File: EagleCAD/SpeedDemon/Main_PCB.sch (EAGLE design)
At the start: 68 parts, among them Q1 DMC2700, U3 LM3676, U4 STM32F072-LQFP48, X1 32.768kHz

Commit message: Draft layout. Moved power reg circuit as far away from everything else as possible to minimize possible noise issues. Also poured polygons for power planes
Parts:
- removed C17: 100nF, rcl:C-US025-024X044
- removed SIGNAL_OP: (no value), wirepad:1,6/0,8
- removed U1A: (no value), US5881:US5881
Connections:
- removed net N$37: SIGNAL_OP.P, U1A.OP
- net GND: no longer C17.2, U1A.VSS
- net VBATT+_SW: no longer C17.1, U1A.VDD
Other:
- note removed: "*NOTE: No PCB for this portion of circuit! Use point-to-point wiring."
- note removed: "3-Conductor cable run"
- note removed: "Sensor module"
- note removed: "Use Mogami W2944 Balanced Console Cable or similar (tie gnd to cable shield)"
- note removed: "XLR-F Cable0 mount conn"
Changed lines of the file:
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@@
 <part name="R32" library="0805_generics" deviceset="R_0805" device="" value="10k"/>
 <part name="GND22" library="supply1" library_urn="urn:adsk.eagle:library:371" deviceset="GND" device=""/>
-<part name="GND23" library="supply1" library_urn="urn:adsk.eagle:library:371" deviceset="GND" device=""/>
-<part name="VBATT_SW3" library="Custom_Power_Inlets" deviceset="VBATT+_SW" device=""/>
-<part name="SIGNAL_OP" library="wirepad" library_urn="urn:adsk.eagle:library:412" deviceset="1,6/0,8" device="" package3d_urn="urn:adsk.eagle:package:30830/1"/>
-<part name="C17" library="rcl" library_urn="urn:adsk.eagle:library:334" deviceset="C-US" device="025-024X044" package3d_urn="urn:adsk.eagle:package:23630/1" value="100nF"/>
-<part name="U1A" library="US5881" deviceset="US5881" device=""/>
-<part name="FRAME2" library="frames" library_urn="urn:adsk.eagle:library:229" deviceset="A3L-LOC" device=""/>
 <part name="C6" library="LCRD_SMD_generics" deviceset="C_0805_NP" device="" value="22pF"/>
 <part name="C18" library="LCRD_SMD_generics" deviceset="C_0805_NP" device="" value="22pF"/>
@@
 </segment>
 </net>
-</nets>
-</sheet>
-<sheet>
-<plain>
-<wire x1="168.275" y1="246.38" x2="168.275" y2="195.58" width="0.1524" layer="97"/>
-<wire x1="168.275" y1="195.58" x2="192.405" y2="195.58" width="0.1524" layer="97"/>
-<wire x1="192.405" y1="195.58" x2="192.405" y2="246.38" width="0.1524" layer="97"/>
-<wire x1="192.405" y1="246.38" x2="168.275" y2="246.38" width="0.1524" layer="97"/>
-<wire x1="103.505" y1="237.49" x2="103.505" y2="203.2" width="0.1524" layer="97"/>
-<wire x1="103.505" y1="203.2" x2="136.525" y2="203.2" width="0.1524" layer="97"/>
-<wire x1="136.525" y1="203.2" x2="136.525" y2="237.49" width="0.1524" layer="97"/>
-<wire x1="136.525" y1="237.49" x2="122.555" y2="237.49" width="0.1524" layer="97"/>
-<text x="104.775" y="238.76" size="1.778" layer="97">Sensor module</text>
-<text x="169.545" y="247.65" size="1.778" layer="97">XLR-F
-Cable0 mount conn</text>
-<wire x1="122.555" y1="237.49" x2="103.505" y2="237.49" width="0.1524" layer="97"/>
-<wire x1="168.275" y1="246.38" x2="168.275" y2="252.73" width="0.1524" layer="97"/>
-<wire x1="168.275" y1="252.73" x2="192.405" y2="252.73" width="0.1524" layer="97"/>
-<wire x1="192.405" y1="252.73" x2="192.405" y2="246.38" width="0.1524" layer="97"/>
-<wire x1="103.505" y1="237.49" x2="103.505" y2="241.3" width="0.1524" layer="97"/>
-<wire x1="103.505" y1="241.3" x2="122.555" y2="241.3" width="0.1524" layer="97"/>
-<wire x1="122.555" y1="241.3" x2="122.555" y2="237.49" width="0.1524" layer="97"/>
-<wire x1="141.605" y1="227.33" x2="141.605" y2="214.63" width="0.1524" layer="97"/>
-<wire x1="141.605" y1="214.63" x2="163.195" y2="214.63" width="0.1524" layer="97"/>
-<wire x1="163.195" y1="214.63" x2="163.195" y2="227.33" width="0.1524" layer="97"/>
-<wire x1="163.195" y1="227.33" x2="156.845" y2="227.33" width="0.1524" layer="97"/>
-<text x="142.875" y="228.6" size="1.778" layer="97">3-Conductor
-cable run</text>
-<wire x1="156.845" y1="227.33" x2="141.605" y2="227.33" width="0.1524" layer="97"/>
-<wire x1="141.605" y1="227.33" x2="141.605" y2="234.95" width="0.1524" layer="97"/>
-<wire x1="141.605" y1="234.95" x2="156.845" y2="234.95" width="0.1524" layer="97"/>
-<wire x1="156.845" y1="234.95" x2="156.845" y2="227.33" width="0.1524" layer="97"/>
-<text x="142.24" y="209.55" size="1.016" layer="97">Use Mogami W2944
-Balanced Console Cable or similar
-(tie gnd to cable shield)</text>
-<text x="98.425" y="253.365" size="1.6764" layer="97">*NOTE: No PCB for this portion of circuit! Use point-to-point wiring.</text>
-</plain>
-<instances>
-<instance part="GND23" gate="1" x="187.325" y="203.2"/>
-<instance part="VBATT_SW3" gate="G$1" x="187.325" y="243.84" smashed="yes">
-<attribute name="VALUE" x="184.785" y="243.84" size="1.778" layer="96" rot="R180"/>
-</instance>
-<instance part="SIGNAL_OP" gate="P" x="187.325" y="220.98" rot="R180"/>
-<instance part="C17" gate="G$1" x="125.095" y="215.9"/>
-<instance part="U1A" gate="G$1" x="111.125" y="220.98"/>
-<instance part="FRAME2" gate="G$1" x="0" y="0"/>
-</instances>
-<busses>
-</busses>
-<nets>
-<net name="VBATT+_SW" class="0">
-<segment>
-<pinref part="VBATT_SW3" gate="G$1" pin="VBATT+_SW"/>
-<wire x1="187.325" y1="241.3" x2="187.325" y2="233.68" width="0.1524" layer="91"/>
-<wire x1="187.325" y1="233.68" x2="165.735" y2="233.68" width="0.1524" layer="91"/>
-<wire x1="165.735" y1="233.68" x2="165.735" y2="224.79" width="0.1524" layer="91"/>
-<wire x1="165.735" y1="224.79" x2="139.065" y2="224.79" width="0.1524" layer="91"/>
-<wire x1="139.065" y1="224.79" x2="139.065" y2="233.68" width="0.1524" layer="91"/>
-<wire x1="139.065" y1="233.68" x2="125.095" y2="233.68" width="0.1524" layer="91"/>
-<pinref part="C17" gate="G$1" pin="1"/>
-<wire x1="125.095" y1="218.44" x2="125.095" y2="233.68" width="0.1524" layer="91"/>
-<wire x1="125.095" y1="233.68" x2="111.125" y2="233.68" width="0.1524" layer="91"/>
-<junction x="125.095" y="233.68"/>
-<pinref part="U1A" gate="G$1" pin="VDD"/>
-</segment>
-</net>
-<net name="N$37" class="0">
-<segment>
-<pinref part="SIGNAL_OP" gate="P" pin="P"/>
-<wire x1="184.785" y1="220.98" x2="121.285" y2="220.98" width="0.1524" layer="91"/>
-<pinref part="U1A" gate="G$1" pin="OP"/>
-</segment>
-</net>
-<net name="GND" class="0">
-<segment>
-<pinref part="GND23" gate="1" pin="GND"/>
-<wire x1="187.325" y1="205.74" x2="187.325" y2="208.28" width="0.1524" layer="91"/>
-<wire x1="187.325" y1="208.28" x2="165.735" y2="208.28" width="0.1524" layer="91"/>
-<wire x1="165.735" y1="208.28" x2="165.735" y2="217.17" width="0.1524" layer="91"/>
-<wire x1="165.735" y1="217.17" x2="139.065" y2="217.17" width="0.1524" layer="91"/>
-<wire x1="139.065" y1="217.17" x2="139.065" y2="208.28" width="0.1524" layer="91"/>
-<pinref part="C17" gate="G$1" pin="2"/>
-<wire x1="125.095" y1="210.82" x2="125.095" y2="208.28" width="0.1524" layer="91"/>
-<junction x="125.095" y="208.28"/>
-<wire x1="125.095" y1="208.28" x2="111.125" y2="208.28" width="0.1524" layer="91"/>
-<pinref part="U1A" gate="G$1" pin="VSS"/>
-<wire x1="125.095" y1="208.28" x2="139.065" y2="208.28" width="0.1524" layer="91"/>
-</segment>
-</net>

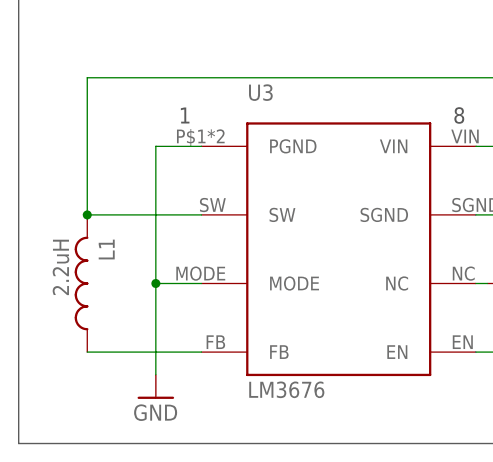
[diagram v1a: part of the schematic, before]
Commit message: fixed inductor choice, picked one that meets spec for the pwr converter
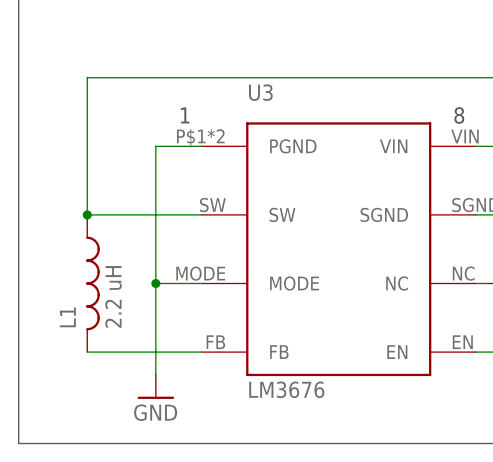
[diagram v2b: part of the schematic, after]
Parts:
- L1: value 2.2uH -> 2.2 uH; device 0805_generics:L_0805 -> LCRD_SMD_generics:NRS4010T2R2MDGGV
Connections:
- net +3V3: now also L1.1; no longer L1.2
- net N$10: now also L1.2; no longer L1.1
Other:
- moved on the sheet: L1
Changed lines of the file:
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@@
 <part name="GND6" library="supply1" library_urn="urn:adsk.eagle:library:371" deviceset="GND" device=""/>
 <part name="+3V4" library="supply1" library_urn="urn:adsk.eagle:library:371" deviceset="+3V3" device=""/>
-<part name="L1" library="0805_generics" deviceset="L_0805" device="" value="2.2uH"/>
 <part name="C1" library="0805_generics" deviceset="C_0805_NP" device="" value="4.7uF"/>
 <part name="C2" library="0805_generics" deviceset="C_0805_NP" device="" value="10uF"/>
@@
 <part name="C20" library="0805_generics" deviceset="C_0805_NP" device="" value="100nF"/>
 <part name="U3" library="LM3676" deviceset="LM3676" device=""/>
+<part name="L1" library="LCRD_SMD_generics" deviceset="NRS4010T2R2MDGGV" device="" value="2.2 uH"/>
 </parts>
 <sheets>
@@
 <instance part="GND6" gate="1" x="76.2" y="12.7"/>
 <instance part="+3V4" gate="G$1" x="106.045" y="246.38"/>
-<instance part="L1" gate="G$1" x="15.24" y="25.4" rot="R180"/>
 <instance part="C1" gate="G$1" x="66.04" y="38.1"/>
 <instance part="C2" gate="G$1" x="76.2" y="43.18"/>
@@
 <instance part="C20" gate="G$1" x="368.3" y="77.47"/>
 <instance part="U3" gate="G$1" x="43.18" y="27.94"/>
+<instance part="L1" gate="G$1" x="15.24" y="25.4"/>
 </instances>
 <busses>
@@
 <wire x1="76.2" y1="45.72" x2="76.2" y2="48.26" width="0.1524" layer="91"/>
 <junction x="76.2" y="48.26"/>
-<pinref part="L1" gate="G$1" pin="2"/>
 <wire x1="27.94" y1="33.02" x2="15.24" y2="33.02" width="0.1524" layer="91"/>
 <wire x1="15.24" y1="33.02" x2="15.24" y2="48.26" width="0.1524" layer="91"/>
+<pinref part="U3" gate="G$1" pin="SW"/>
+<pinref part="L1" gate="G$1" pin="1"/>
 <junction x="15.24" y="33.02"/>
-<pinref part="U3" gate="G$1" pin="SW"/>
 </segment>
 <segment>
@@
 <net name="N$10" class="0">
 <segment>
-<pinref part="L1" gate="G$1" pin="1"/>
 <wire x1="15.24" y1="17.78" x2="27.94" y2="17.78" width="0.1524" layer="91"/>
 <pinref part="U3" gate="G$1" pin="FB"/>
-</segment>
-</net>
+<pinref part="L1" gate="G$1" pin="2"/>
+</segment>
+</net>

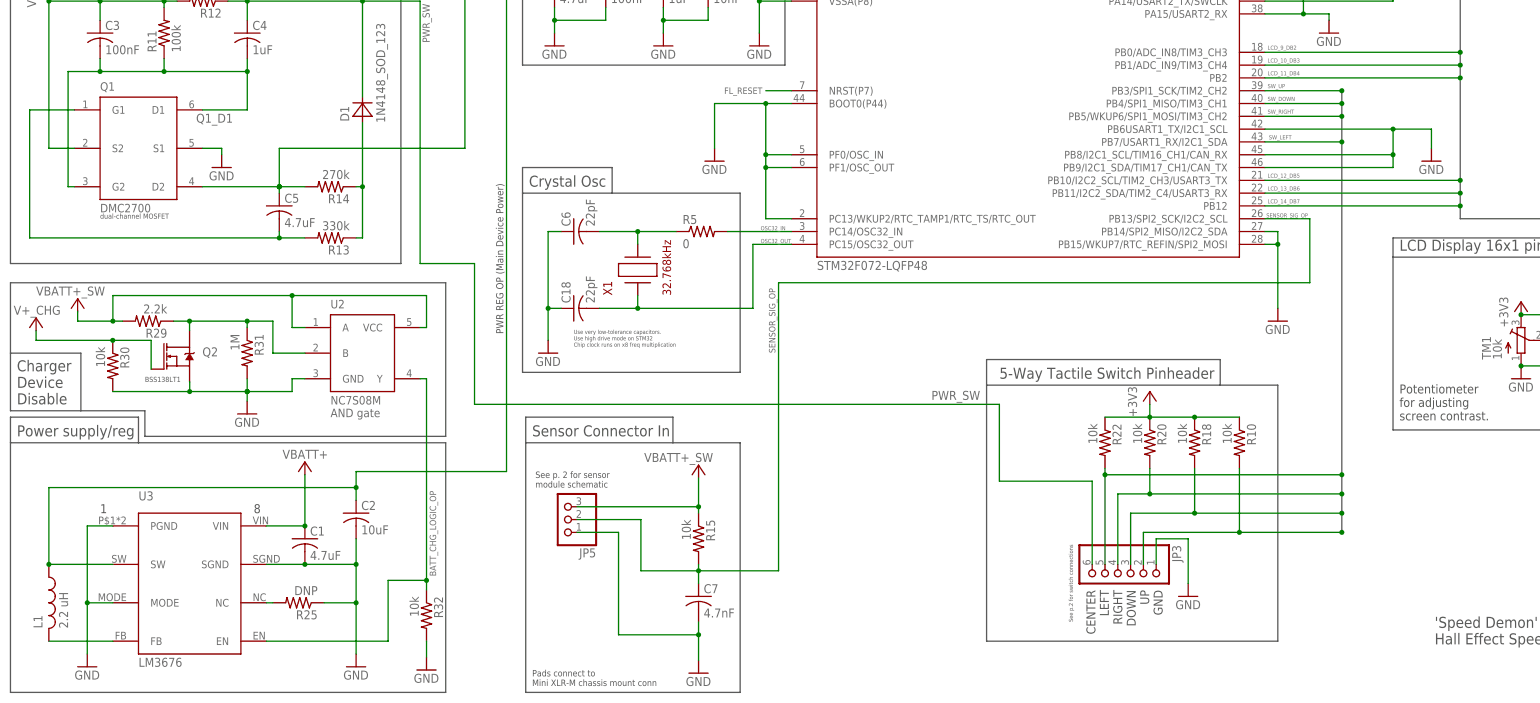
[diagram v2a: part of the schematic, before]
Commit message: updated schematic/layout with pwr inlet debounce circuit and added center switch connectivity to MCU. Other small organizational changes.
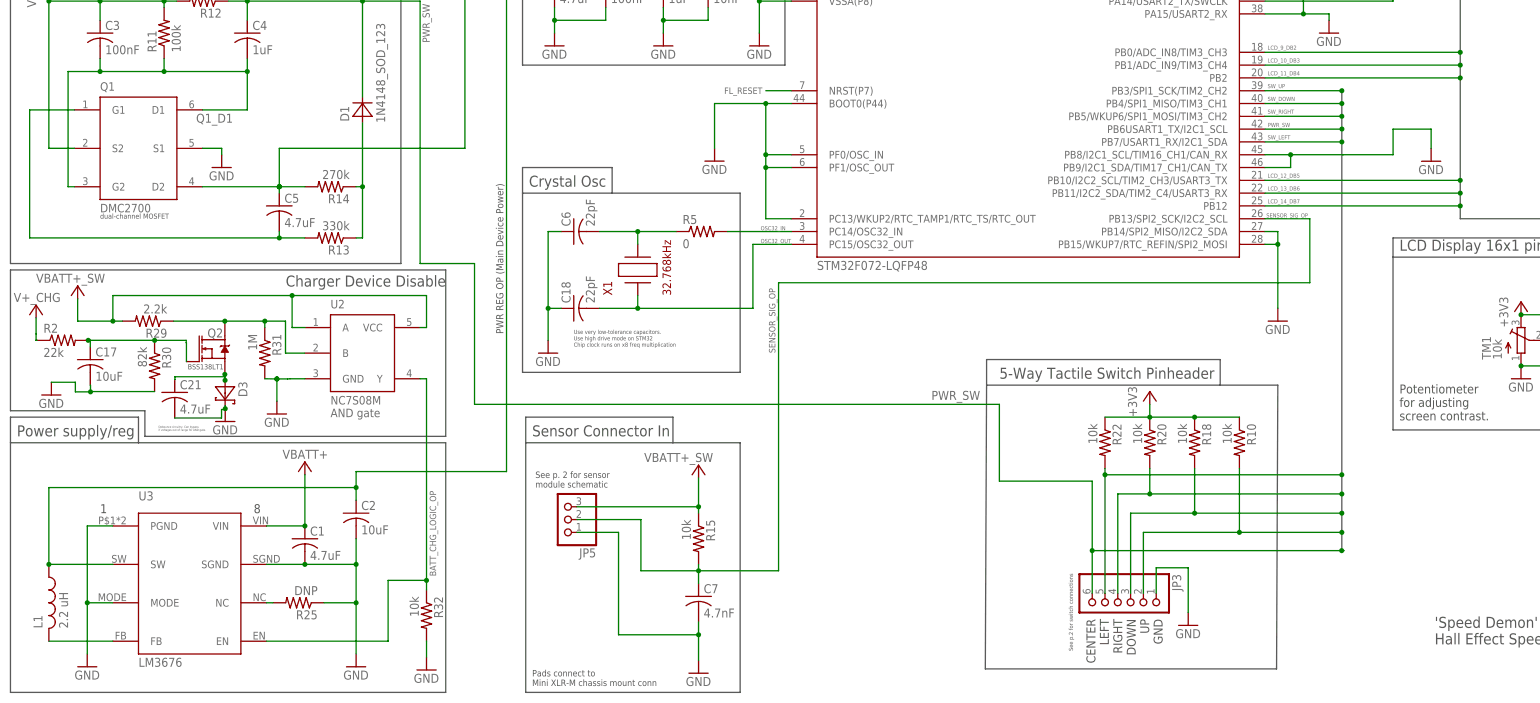
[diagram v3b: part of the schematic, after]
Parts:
- added C17: 10uF, 0805_generics:C_0805_NP
- added C21: 4.7uF, 0805_generics:C_0805_NP
- added D3: (no value), LCRD_SMD_generics:CFSH05_SCHOTTKY
- added R2: 22k, 0805_generics:R_0805
- R30: value 10k -> 82k
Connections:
- new net N$12: C17.1, Q2.G, R2.2, R30.1
- new net N$16: C21.1, D3.A, Q2.S
- net +V+_CHG: now also R2.1; no longer Q2.G, R30.1
- net GND: now also C17.2, C21.2, D3.C; no longer Q2.S, U4.PB6USART1_TX/I2C1_SCL
- net PWR_SW: now also U4.PB6USART1_TX/I2C1_SCL
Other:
- note added: "Debounce circuitry. Can bypass if voltages out of range for AND gate."
- moved on the sheet: JP3, Q2, R30, R31

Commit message: Added WPRs, finished changes for debounce circuit.
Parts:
- added D4: (no value), LCRD_SMD_generics:CFSH05_SCHOTTKY
- added R6: 1k, 0805_generics:R_0805
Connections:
- new net N$11: D4.C, R6.1, U2.B
- net GND: now also R6.2
- net N$28: now also D4.A; no longer U2.B
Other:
- moved on the sheet: R31, U2
